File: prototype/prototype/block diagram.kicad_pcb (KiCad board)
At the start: 2 copper layers, 7 parts, among them U1 AMS1117-3.3, U11 ESP32-WROOM-32E, U3 MQ-6, U8 CI121S021 [adc], U9 MQ-4M

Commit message: final schematic organized
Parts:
- removed D1: IRL81A, LED_THT:LED_SideEmitter_Rectangular_W4.5mm_H1.6mm
- removed U3: MQ-6, Sensor:MQ-6
- removed U9: MQ-4M, Sensor:MQ-6
- added C10: 10uF, Photon:C0603, F.Cu at (245.2, 123.0)
- added C11: 10uF, Photon:C0603, F.Cu at (245.2, 125.7)
- added C12: 10uF, Photon:C0603, F.Cu at (245.2, 128.4)
- added C2: 10nF, Photon:C0603, F.Cu at (241.2, 117.7)
- added C3: 1uF, Photon:C0603, F.Cu at (241.2, 120.4)
- added C4: 0.1uF, Photon:C0603, F.Cu at (241.2, 123.0)
- added C5: 220uF, Photon:C0603, F.Cu at (241.2, 125.7)
- added C6: 1uF, Photon:C0603, F.Cu at (241.2, 128.4)
- added C7: 0.1uF, Photon:C0603, F.Cu at (245.2, 117.7)
- added C8: 22uF, Photon:C0603, F.Cu at (245.2, 120.4)
- added D3: 1N4148, Diode_THT:D_DO-35_SOD27_P7.62mm_Horizontal, F.Cu at (240.7, 131.5)
- added F1: 0.5A, Photon:Fuse_1206_3216Metric, F.Cu at (251.8, 141.5)
- added L1: 10mH, Photon:L_APV_ANR5040, F.Cu at (252.3, 136.6)
- added R1: 4.7k, Photon:R_0603_1608Metric_Pad0.98x0.95mm_HandSolder, F.Cu at (241.3, 102.6)
- added R10: 10k, Photon:R_0603_1608Metric_Pad0.98x0.95mm_HandSolder, F.Cu at (241.3, 115.1)
- added R16: 4.7k, Photon:R_0603_1608Metric_Pad0.98x0.95mm_HandSolder, F.Cu at (245.7, 102.6)
- added R17: 4.7k, Photon:R_0603_1608Metric_Pad0.98x0.95mm_HandSolder, F.Cu at (245.7, 105.1)
- added R18: 330, Photon:R_0603_1608Metric_Pad0.98x0.95mm_HandSolder, F.Cu at (245.7, 107.6)
- added R19: 330, Photon:R_0603_1608Metric_Pad0.98x0.95mm_HandSolder, F.Cu at (245.7, 110.1)
- added R2: 4.7k, Photon:R_0603_1608Metric_Pad0.98x0.95mm_HandSolder, F.Cu at (241.3, 105.1)
- added R20: 10k, Photon:R_0603_1608Metric_Pad0.98x0.95mm_HandSolder, F.Cu at (245.7, 112.6)
- added R7: 4.7k, Photon:R_0603_1608Metric_Pad0.98x0.95mm_HandSolder, F.Cu at (241.3, 107.6)
- added R8: 4.7k, Photon:R_0603_1608Metric_Pad0.98x0.95mm_HandSolder, F.Cu at (241.3, 110.1)
- added R9: 100, Photon:R_0603_1608Metric_Pad0.98x0.95mm_HandSolder, F.Cu at (241.3, 112.6)
- added RV1: 10D561, Photon:RV_Disc_D7mm_W5.7mm_P5mm, F.Cu at (249.0, 118.5)
- added U5: MQ-5, Sensor:MQ-6, F.Cu at (148.8, 66.8)
- moved U8 87.1 mm to (249.8, 126.0), turned to 0 degrees
- moved U1 60.7 mm to (244.1, 137.5), turned to 0 degrees
- moved U11 40.9 mm to (194.2, 86.7)
- moved PS1 12.0 mm to (140.9, 121.5)
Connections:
- net 3v3 renamed +3.3V
- net 5v renamed +5V
- U11 pad 27: Net-(U11-IO16) -> /IO_16_Detect
- U8 pad 3: /A_O -> /Sensor_A_O

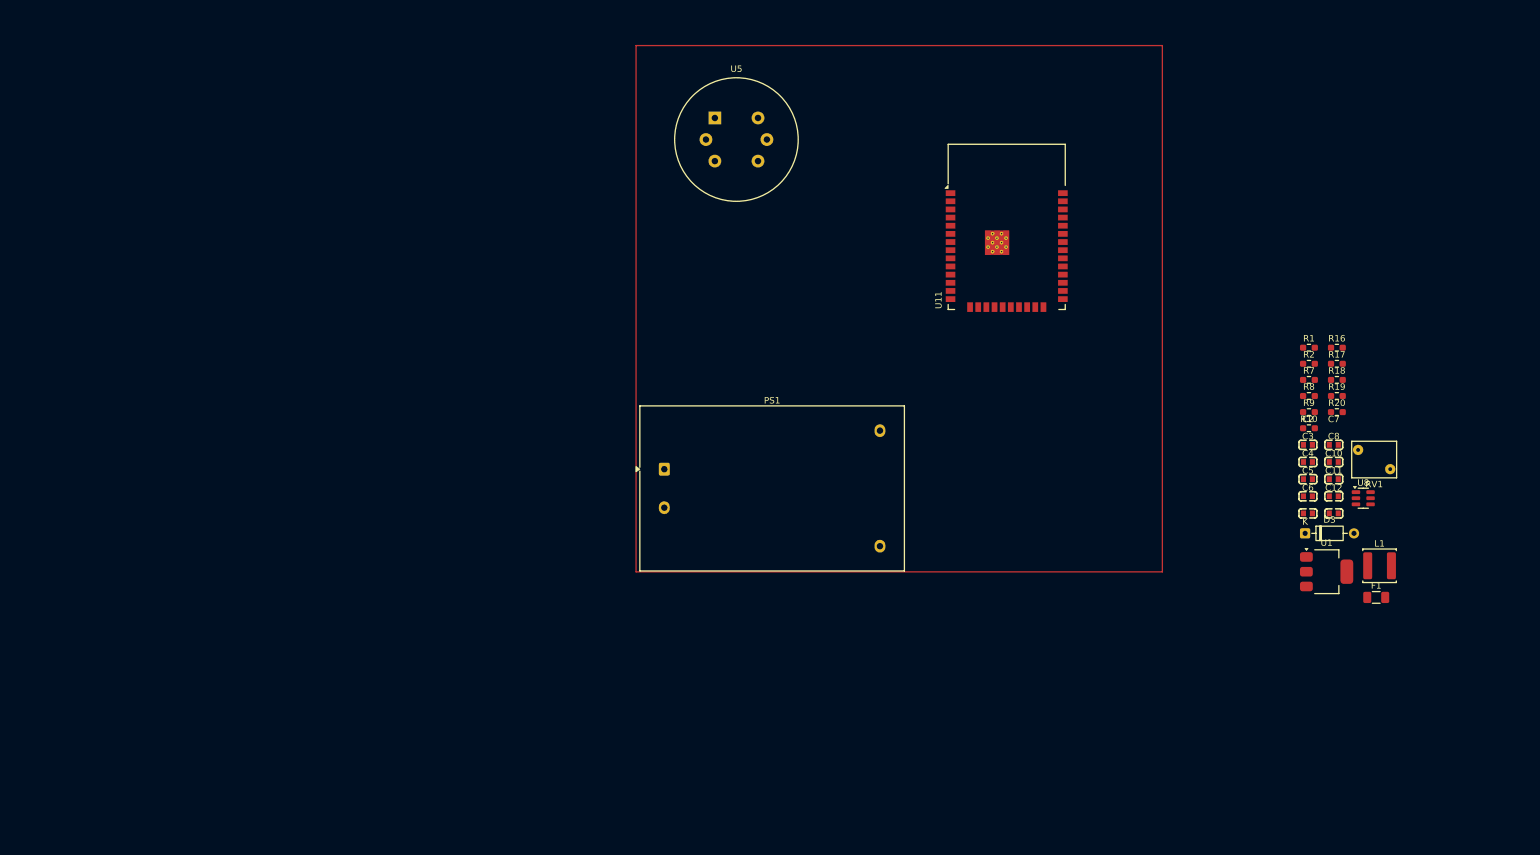
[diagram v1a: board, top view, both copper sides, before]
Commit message: updated footprints
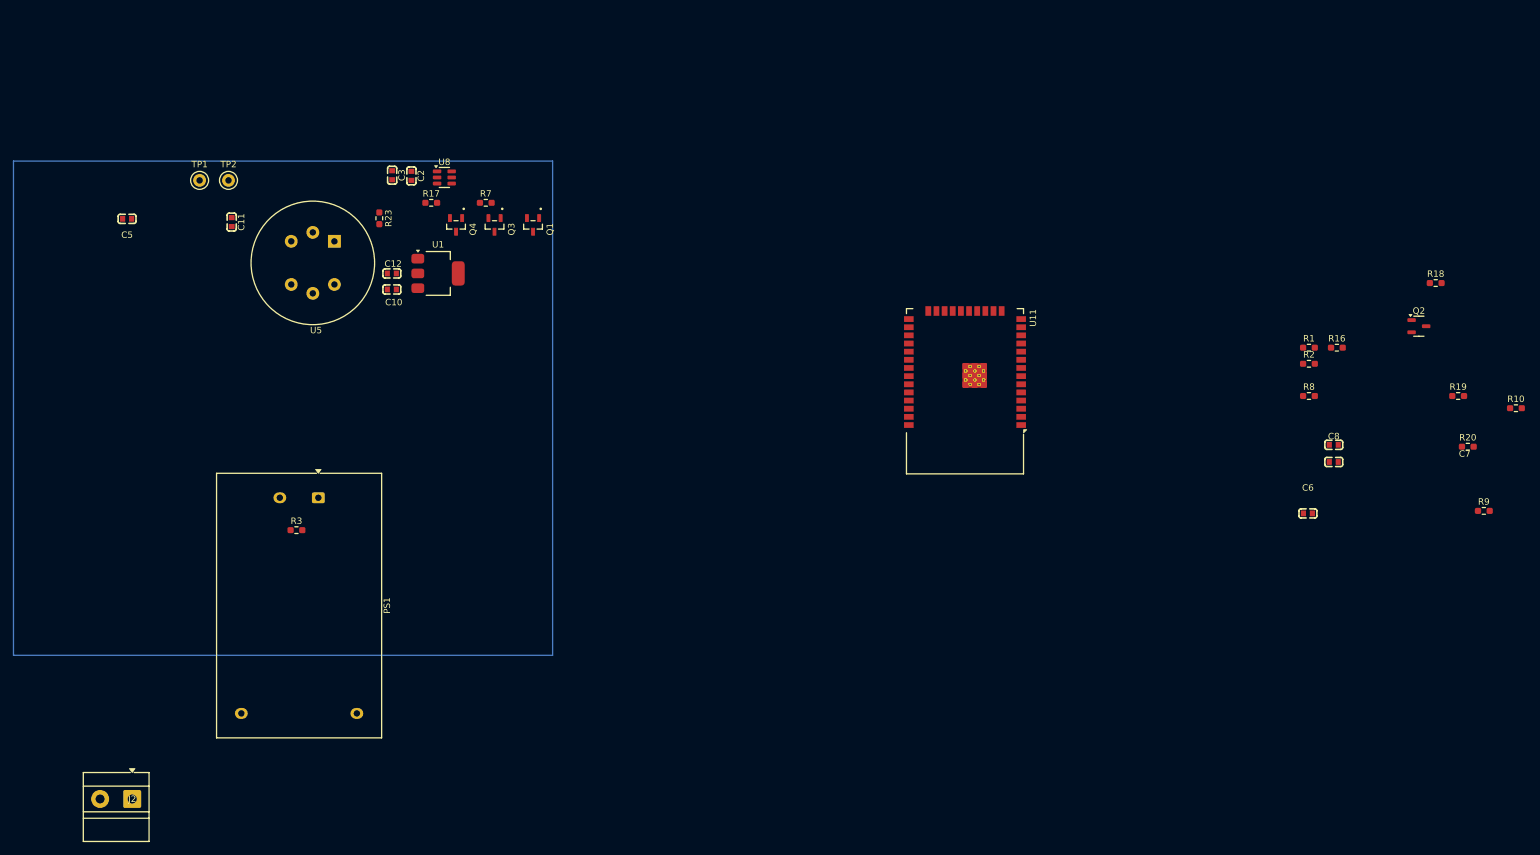
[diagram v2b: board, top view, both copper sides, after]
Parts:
- removed C4: 0.1uF, Photon:C0603
- removed D3: 1N4148, Diode_THT:D_DO-35_SOD27_P7.62mm_Horizontal
- removed F1: 0.5A, Photon:Fuse_1206_3216Metric
- removed L1: 10mH, Photon:L_APV_ANR5040
- removed RV1: 10D561, Photon:RV_Disc_D7mm_W5.7mm_P5mm
- added J2: Screw_Terminal_01x02, TerminalBlock_MetzConnect:TerminalBlock_MetzConnect_Type011_RT05502HBLC_1x02_P5.00mm_Horizontal, F.Cu at (58.0, 172.9)
- added Q1: 2N7002, Photon:SOT95P240X111-3N, F.Cu at (120.5, 83.4)
- added Q2: AO3400, Package_TO_SOT_SMD:SOT-23-3, F.Cu at (258.5, 99.2)
- added Q3: 2N7002, Photon:SOT95P240X111-3N, F.Cu at (114.5, 83.4)
- added Q4: 2N7002, Photon:SOT95P240X111-3N, F.Cu at (108.5, 83.4)
- added R23: 20k, Photon:R_0603_1608Metric_Pad0.98x0.95mm_HandSolder, F.Cu at (96.5, 82.4)
- added R3: 1k, Photon:R_0603_1608Metric_Pad0.98x0.95mm_HandSolder, F.Cu at (83.6, 131.0)
- added TP1: TestPoint, TestPoint:TestPoint_Keystone_5000-5004_Miniature, F.Cu at (68.5, 76.5)
- added TP2: TestPoint, TestPoint:TestPoint_Keystone_5000-5004_Miniature, F.Cu at (73.0, 76.5)
- moved C5 189.0 mm to (57.2, 82.5)
- moved C11 176.9 mm to (73.5, 83.0), turned to -90 degrees
- moved U8 151.6 mm to (106.6, 76.0)
- moved C12 151.4 mm to (98.5, 91.0), turned to 180 degrees
- moved C10 149.7 mm to (98.5, 93.5), turned to 180 degrees
- moved C3 149.5 mm to (98.5, 75.7), turned to -90 degrees
- moved U1 146.0 mm to (105.7, 91.0)
- moved C2 145.8 mm to (101.5, 75.8), turned to -90 degrees
- moved R17 143.3 mm to (104.6, 80.0)
- moved R7 131.2 mm to (113.1, 80.0)
- moved U5 62.3 mm to (89.5, 86.0), turned to -90 degrees
- moved PS1 54.1 mm to (87.0, 126.0), turned to -90 degrees
- moved R10 32.4 mm to (273.6, 112.0)
- moved R9 31.3 mm to (268.6, 128.0)
- moved R18 21.6 mm to (261.1, 92.5)
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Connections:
- PS1 pad 1: Net-(PS1-AC/L) -> /L
- PS1 pad 2: Net-(PS1-AC/N) -> /N
- R18 pad 1: /ESP_EN -> /STATUS_LED
- U11 pad 31: unconnected-(U11-IO19-Pad31) -> /STATUS_LED

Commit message: pcb layout and updated led
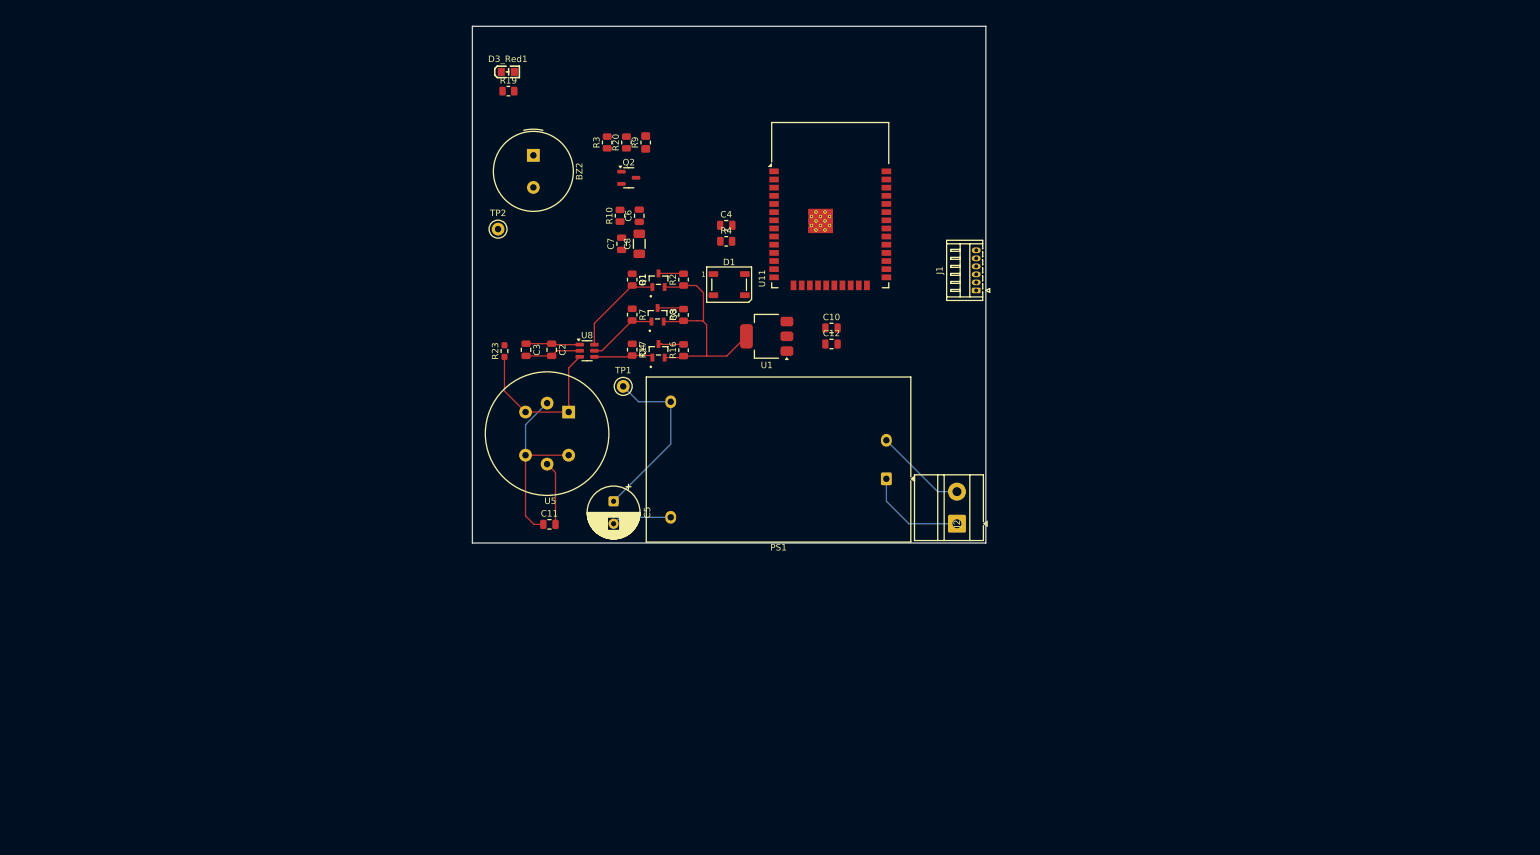
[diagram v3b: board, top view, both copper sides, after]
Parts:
- removed R18: 330, Photon:R_0603_1608Metric_Pad0.98x0.95mm_HandSolder
- added BZ2: Buzzer, Photon:Buzzer_TDK_PS1240P02BT_D12.2mm_H6.5mm, F.Cu at (120.5, 72.6)
- added C4: 0.1uF, Photon:C_0805_2012Metric, F.Cu at (150.6, 83.5)
- added D1: WS2812B, LED_SMD:LED_WS2812B_PLCC4_5.0x5.0mm_P3.2mm, F.Cu at (151.0, 92.8)
- added D3_Red1: LED, Photon:LED-SMD_L2.0-W1.25-RD-GREEN, F.Cu at (116.5, 59.6)
- added J1: Conn_01x06_Pin, Connector_Hirose:Hirose_DF13-06P-1.25DS_1x06_P1.25mm_Horizontal, F.Cu at (189.5, 93.7)
- added R4: 330, Photon:R_0805_2012Metric, F.Cu at (150.6, 86.0)
- C10, C11, C12, C2, C3, C6, C7: footprint Photon:C0603 -> Photon:C_0805_2012Metric
- C5: footprint Photon:C0603 -> Photon:CP_Radial_D8.0mm_P3.50mm
- C8: footprint Photon:C0603 -> Photon:C_1206_3216Metric_Pad1.33x1.80mm_HandSolder
- R1, R10, R16, R17, R19, R2, R20, R3, R7, R8: footprint Photon:R_0603_1608Metric_Pad0.98x0.95mm_HandSolder -> Photon:R_0805_2012Metric
- R9: footprint Photon:R_0603_1608Metric_Pad0.98x0.95mm_HandSolder -> Photon:R_0805_2012Metric_Pad1.20x1.40mm_HandSolder
- TP1: value TestPoint -> 5v
- TP2: value TestPoint -> gnd
- moved R19 155.4 mm to (116.6, 62.6)
- moved R10 142.8 mm to (134.0, 82.0), turned to 90 degrees
- moved R9 142.6 mm to (138.0, 70.6), turned to 90 degrees
- moved R20 139.4 mm to (135.0, 70.6), turned to 90 degrees
- moved J2 135.5 mm to (186.5, 130.0), turned to 90 degrees
- moved Q2 125.3 mm to (135.4, 76.1)
- moved C7 115.3 mm to (134.2, 86.4), turned to 90 degrees
- moved C6 114.0 mm to (137.0, 82.0), turned to 90 degrees
- moved C8 113.4 mm to (137.0, 86.4), turned to 90 degrees
- moved R1 106.0 mm to (135.9, 92.0), turned to -90 degrees
- moved R16 101.8 mm to (143.9, 103.0), turned to 90 degrees
- moved R2 98.3 mm to (143.9, 92.0), turned to 90 degrees
- moved R8 98.3 mm to (143.9, 97.5), turned to 90 degrees
- moved PS1 88.5 mm to (175.5, 123.0), turned to 180 degrees
- moved C5 87.6 mm to (133.0, 126.5), turned to -90 degrees
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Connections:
- net /IO_16_Detect renamed /IO_16_on
- U11 pad 10: unconnected-(U11-IO25-Pad10) -> /BUZZ_OUT
- U11 pad 12: unconnected-(U11-IO27-Pad12) -> /STATUS_LED
- U11 pad 31: /STATUS_LED -> unconnected-(U11-IO19-Pad31)
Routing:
- net +5V: track 0.00 -> 65.0 mm
- net +3.3V: track 0.00 -> 37.1 mm
- net GND: track 0.00 -> 27.9 mm
- net /Sensor_A_O: track 0.00 -> 26.0 mm
- net /L: track 0.00 -> 15.9 mm
- net /CS_5: track 0.00 -> 15.4 mm
- net /N: track 0.00 -> 14.3 mm
- net /SDATA_5: track 0.07 -> 10.9 mm
- net /CLK_5: track 0.00 -> 9.27 mm
- net /SDATA_3: track 0.00 -> 4.12 mm
- net /CS_3: track 0.00 -> 3.92 mm
- net /CLK_3: track 0.00 -> 3.92 mm
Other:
- board outline added: 80 x 80.5 mm

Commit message: pcb layout almost complete
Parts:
- R23: footprint Photon:R_0603_1608Metric_Pad0.98x0.95mm_HandSolder -> Photon:R_0805_2012Metric
- moved J1 8.03 mm to (185.9, 86.5), turned to -90 degrees
- moved C4 4.37 mm to (148.8, 87.5)
- moved R4 3.12 mm to (153.3, 87.5), turned to 180 degrees
- moved C11 1.60 mm to (123.0, 128.5)
- moved C10 1.17 mm to (166.8, 98.3)
- moved C12 1.17 mm to (166.8, 100.8)
- moved Q2 0.96 mm to (135.0, 75.2), turned to 90 degrees
- turned D3_Red1 to 180 degrees
- turned R19 to 180 degrees
- turned R3 to -90 degrees
- turned R9 to -90 degrees
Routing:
- net +5V: track 65.0 -> 221.8 mm, vias 0 -> 4
- net /BUZZ_OUT: track 0.00 -> 28.8 mm
- net Net-(BZ2--): track 0.00 -> 20.8 mm
- net Net-(Q2-G): track 0.00 -> 9.13 mm
- net GND: track 27.9 -> 36.3 mm
- net +3.3V: track 37.1 -> 42.8 mm, vias 0 -> 3
- net /STATUS_LED: track 0.00 -> 4.45 mm
- net Net-(D1-DIN): track 0.00 -> 4.05 mm

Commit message: editing pcb layout (desktop)
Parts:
- added TP3: 3v3, TestPoint:TestPoint_Keystone_5000-5004_Miniature, F.Cu at (143.0, 85.0)
- moved C7 15.9 mm to (147.8, 77.9), turned to -90 degrees
- moved C8 15.5 mm to (150.5, 78.7), turned to -90 degrees
- moved R10 14.4 mm to (148.2, 84.0)
- moved C6 13.9 mm to (150.8, 84.0), turned to -90 degrees
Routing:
- net +3.3V: track 42.8 -> 92.4 mm, vias 3 -> 4
- net /ESP_EN: track 0.00 -> 12.0 mm
- net /BUZZ_OUT: vias 0 -> 2

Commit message: finished pcb prototype
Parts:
- moved R19 20.5 mm to (136.9, 59.5)
- turned D3_Red1 to 0 degrees
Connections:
- J1 pad 3: /ESP_IO0 -> /ESP_TXD0
- J1 pad 4: /ESP_TXD0 -> /ESP_RXD0
- J1 pad 5: /ESP_RDD0 -> /ESP_IO0
- U11 pad 27: /IO_16_on -> unconnected-(U11-IO16-Pad27)
- U11 pad 28: /SDATA_3 -> /CLK_3
- U11 pad 30: /CLK_3 -> /SDATA_3
- U11 pad 9: unconnected-(U11-IO33-Pad9) -> /IO_16_on
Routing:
- net /IO_16_on: track 0.00 -> 40.8 mm, vias 0 -> 2
- net /CLK_3: track 3.92 -> 42.1 mm
- net /SDATA_3: track 4.12 -> 40.4 mm
- net /ESP_EN: track 12.0 -> 46.7 mm, vias 0 -> 2
- net +3.3V: track 92.4 -> 124.6 mm, vias 4 -> 6
- net /ESP_TXD0: track 0.00 -> 18.7 mm
- net Net-(D3_Red1-A): track 0.00 -> 18.5 mm
- net /ESP_RXD0: track 0.00 -> 17.5 mm
- net /CS_3: track 3.92 -> 21.3 mm
- net /ESP_IO0: track 0.00 -> 10.5 mm
- net +5V: track 221.8 -> 219.2 mm
- added copper zone on F.Cu, net GND

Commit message: FINAL FINAL PCB
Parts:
- removed C11: 10uF, Photon:C_0805_2012Metric
- removed TP2: gnd, TestPoint:TestPoint_Keystone_5000-5004_Miniature
- added C2: 10uF, Photon:C_0805_2012Metric, F.Cu at (123.0, 128.2)
- J1: footprint Connector_Hirose:Hirose_DF13-06P-1.25DS_1x06_P1.25mm_Horizontal -> Connector_JST:JST_EH_S6B-EH_1x06_P2.50mm_Horizontal
- moved J1 2.29 mm to (183.8, 85.7)
- renumbered TP3 to 3V3, TP1 to 5V, BZ2 to BZ1, C5 to C1, C12 to C10, C2 to C3, C3 to C4, C4 to C5, C10 to C9, D3_Red1 to D2, Q4 to Q1, Q3 to Q2, Q1 to Q3, Q2 to Q4, R23 to R1, R9 to R10, R20 to R11, R3 to R12, R19 to R13, R17 to R2, R16 to R3, R7 to R4, R8 to R5, R1 to R6, R2 to R7, R10 to R8, R4 to R9, U5 to U1, U8 to U2, U1 to U3
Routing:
- net +5V: track 219.2 -> 252.5 mm, vias 4 -> 5
- net GND: track 36.3 -> 27.3 mm, vias 0 -> 230
- net +3.3V: track 124.6 -> 128.8 mm
- net /L: track 15.9 -> 13.9 mm
- net /IO_16_on: track 40.8 -> 42.8 mm
- net /ESP_TXD0: track 18.7 -> 16.8 mm
- net /ESP_EN: track 46.7 -> 45.0 mm
- net /CLK_3: track 42.1 -> 41.4 mm, vias 0 -> 2
- net /CS_5: track 15.4 -> 14.9 mm
- added copper zone on B.Cu, net GND

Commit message: FINAL FINAL PCB TO BE SENT
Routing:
- net GND: vias 230 -> 36
